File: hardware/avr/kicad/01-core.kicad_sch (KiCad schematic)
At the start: 18 parts, among them U1 ATmega1284P-PU, Y1 8MHz

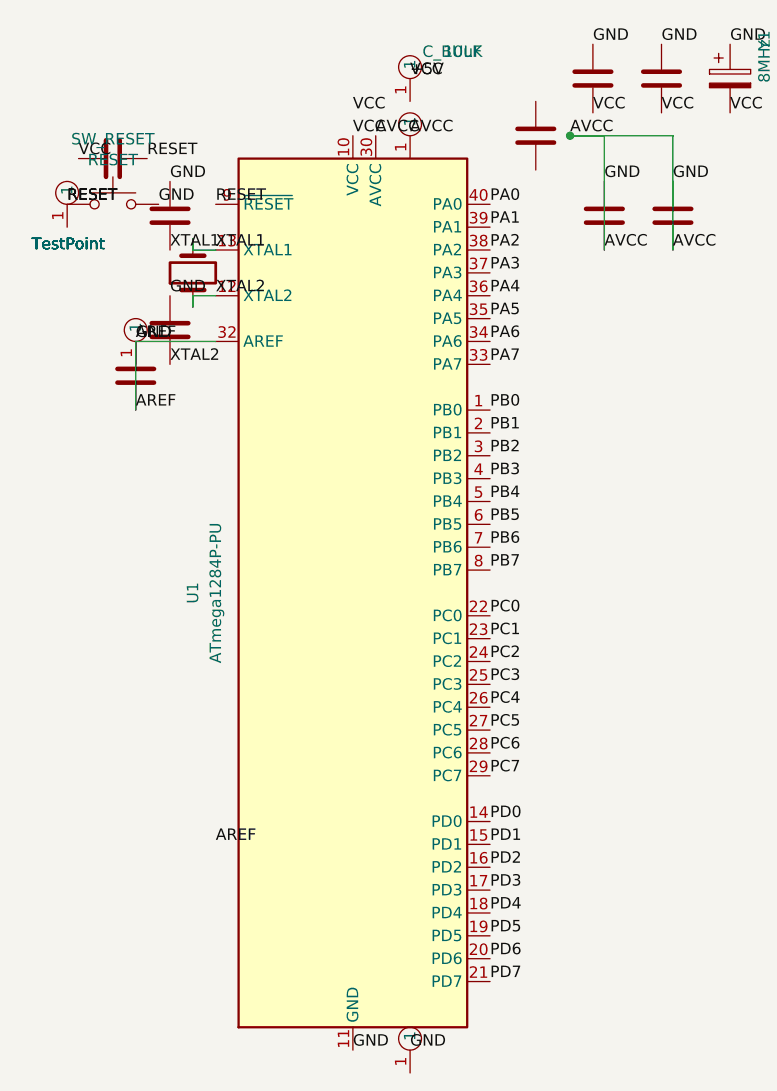
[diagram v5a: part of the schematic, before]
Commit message: Normalize embedded AVR symbol pin geometry
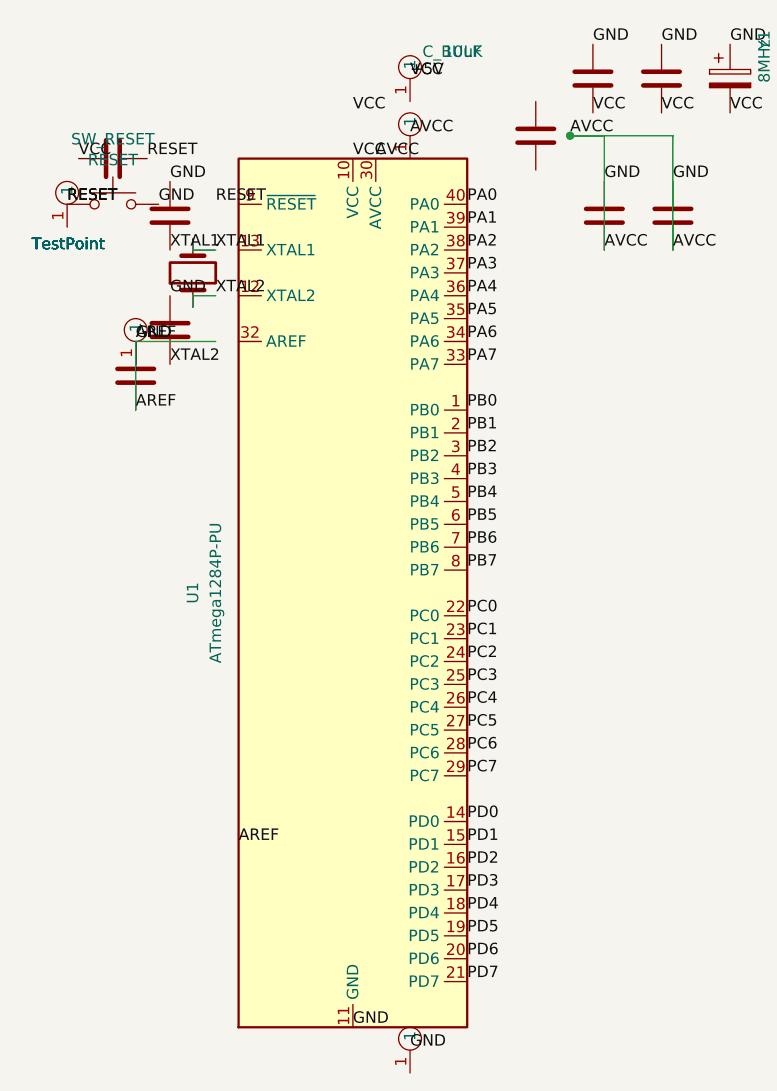
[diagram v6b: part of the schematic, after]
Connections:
- net AREF: no longer U1.32 (AREF)
- net RESET: no longer U1.9 (~{RESET})
- net XTAL1: no longer U1.13 (XTAL1)
- net XTAL2: no longer U1.12 (XTAL2)
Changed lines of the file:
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@@
 (kicad_sch (version 20230121) (generator eeschema)
   (paper "A4")
-  (label "VCC" (at 57.15 29.21 0) (fields_autoplaced)
-    (effects (font (size 1.27 1.27)) (justify left bottom))
-  )
-  (label "GND" (at 57.15 130.81 0) (fields_autoplaced)
-    (effects (font (size 1.27 1.27)) (justify left bottom))
-  )
-  (label "AVCC" (at 59.69 29.21 0) (fields_autoplaced)
-    (effects (font (size 1.27 1.27)) (justify left bottom))
-  )
-  (label "AREF" (at 41.91 107.95 0) (fields_autoplaced)
+  (label "VCC" (at 57.15 31.75 0) (fields_autoplaced)
+    (effects (font (size 1.27 1.27)) (justify left bottom))
+  )
+  (label "GND" (at 57.15 128.27 0) (fields_autoplaced)
+    (effects (font (size 1.27 1.27)) (justify left bottom))
+  )
+  (label "AVCC" (at 59.69 31.75 0) (fields_autoplaced)
+    (effects (font (size 1.27 1.27)) (justify left bottom))
+  )
+  (label "AREF" (at 44.45 107.95 0) (fields_autoplaced)
     (effects (font (size 1.27 1.27)) (justify left bottom))
   )
@@
     )
   )
-  (label "PA0" (at 72.39 36.83 0) (fields_autoplaced)
-    (effects (font (size 1.27 1.27)) (justify left bottom))
-  )
-  (label "PA1" (at 72.39 39.37 0) (fields_autoplaced)
-    (effects (font (size 1.27 1.27)) (justify left bottom))
-  )
-  (label "PA2" (at 72.39 41.91 0) (fields_autoplaced)
-    (effects (font (size 1.27 1.27)) (justify left bottom))
-  )
-  (label "PA3" (at 72.39 44.45 0) (fields_autoplaced)
-    (effects (font (size 1.27 1.27)) (justify left bottom))
-  )
-  (label "PA4" (at 72.39 46.99 0) (fields_autoplaced)
-    (effects (font (size 1.27 1.27)) (justify left bottom))
-  )
-  (label "PA5" (at 72.39 49.53 0) (fields_autoplaced)
-    (effects (font (size 1.27 1.27)) (justify left bottom))
-  )
-  (label "PA6" (at 72.39 52.07 0) (fields_autoplaced)
-    (effects (font (size 1.27 1.27)) (justify left bottom))
-  )
-  (label "PA7" (at 72.39 54.61 0) (fields_autoplaced)
-    (effects (font (size 1.27 1.27)) (justify left bottom))
-  )
-  (label "PB0" (at 72.39 59.69 0) (fields_autoplaced)
-    (effects (font (size 1.27 1.27)) (justify left bottom))
-  )
-  (label "PB1" (at 72.39 62.23 0) (fields_autoplaced)
-    (effects (font (size 1.27 1.27)) (justify left bottom))
-  )
-  (label "PB2" (at 72.39 64.77 0) (fields_autoplaced)
-    (effects (font (size 1.27 1.27)) (justify left bottom))
-  )
-  (label "PB3" (at 72.39 67.31 0) (fields_autoplaced)
-    (effects (font (size 1.27 1.27)) (justify left bottom))
-  )
-  (label "PB4" (at 72.39 69.85 0) (fields_autoplaced)
-    (effects (font (size 1.27 1.27)) (justify left bottom))
-  )
-  (label "PB5" (at 72.39 72.39 0) (fields_autoplaced)
-    (effects (font (size 1.27 1.27)) (justify left bottom))
-  )
-  (label "PB6" (at 72.39 74.93 0) (fields_autoplaced)
-    (effects (font (size 1.27 1.27)) (justify left bottom))
-  )
-  (label "PB7" (at 72.39 77.47 0) (fields_autoplaced)
-    (effects (font (size 1.27 1.27)) (justify left bottom))
-  )
-  (label "PC0" (at 72.39 82.55 0) (fields_autoplaced)
-    (effects (font (size 1.27 1.27)) (justify left bottom))
-  )
-  (label "PC1" (at 72.39 85.09 0) (fields_autoplaced)
-    (effects (font (size 1.27 1.27)) (justify left bottom))
-  )
-  (label "PC2" (at 72.39 87.63 0) (fields_autoplaced)
-    (effects (font (size 1.27 1.27)) (justify left bottom))
-  )
-  (label "PC3" (at 72.39 90.17 0) (fields_autoplaced)
-    (effects (font (size 1.27 1.27)) (justify left bottom))
-  )
-  (label "PC4" (at 72.39 92.71 0) (fields_autoplaced)
-    (effects (font (size 1.27 1.27)) (justify left bottom))
-  )
-  (label "PC5" (at 72.39 95.25 0) (fields_autoplaced)
-    (effects (font (size 1.27 1.27)) (justify left bottom))
-  )
-  (label "PC6" (at 72.39 97.79 0) (fields_autoplaced)
-    (effects (font (size 1.27 1.27)) (justify left bottom))
-  )
-  (label "PC7" (at 72.39 100.33 0) (fields_autoplaced)
-    (effects (font (size 1.27 1.27)) (justify left bottom))
-  )
-  (label "PD0" (at 72.39 105.41 0) (fields_autoplaced)
-    (effects (font (size 1.27 1.27)) (justify left bottom))
-  )
-  (label "PD1" (at 72.39 107.95 0) (fields_autoplaced)
-    (effects (font (size 1.27 1.27)) (justify left bottom))
-  )
-  (label "PD2" (at 72.39 110.49 0) (fields_autoplaced)
-    (effects (font (size 1.27 1.27)) (justify left bottom))
-  )
-  (label "PD3" (at 72.39 113.03 0) (fields_autoplaced)
-    (effects (font (size 1.27 1.27)) (justify left bottom))
-  )
-  (label "PD4" (at 72.39 115.57 0) (fields_autoplaced)
-    (effects (font (size 1.27 1.27)) (justify left bottom))
-  )
-  (label "PD5" (at 72.39 118.11 0) (fields_autoplaced)
-    (effects (font (size 1.27 1.27)) (justify left bottom))
-  )
-  (label "PD6" (at 72.39 120.65 0) (fields_autoplaced)
-    (effects (font (size 1.27 1.27)) (justify left bottom))
-  )
-  (label "PD7" (at 72.39 123.19 0) (fields_autoplaced)
-    (effects (font (size 1.27 1.27)) (justify left bottom))
-  )
+  (label "PA0" (at 69.85 36.83 0) (fields_autoplaced)
+    (effects (font (size 1.27 1.27)) (justify left bottom))
+  )
+  (label "PA1" (at 69.85 39.37 0) (fields_autoplaced)
+    (effects (font (size 1.27 1.27)) (justify left bottom))
+  )
+  (label "PA2" (at 69.85 41.91 0) (fields_autoplaced)
+    (effects (font (size 1.27 1.27)) (justify left bottom))
+  )
+  (label "PA3" (at 69.85 44.45 0) (fields_autoplaced)
+    (effects (font (size 1.27 1.27)) (justify left bottom))
+  )
+  (label "PA4" (at 69.85 46.99 0) (fields_autoplaced)
+    (effects (font (size 1.27 1.27)) (justify left bottom))
+  )
+  (label "PA5" (at 69.85 49.53 0) (fields_autoplaced)
+    (effects (font (size 1.27 1.27)) (justify left bottom))
+  )
+  (label "PA6" (at 69.85 52.07 0) (fields_autoplaced)
+    (effects (font (size 1.27 1.27)) (justify left bottom))
+  )
+  (label "PA7" (at 69.85 54.61 0) (fields_autoplaced)
+    (effects (font (size 1.27 1.27)) (justify left bottom))
+  )
+  (label "PB0" (at 69.85 59.69 0) (fields_autoplaced)
+    (effects (font (size 1.27 1.27)) (justify left bottom))
+  )
+  (label "PB1" (at 69.85 62.23 0) (fields_autoplaced)
+    (effects (font (size 1.27 1.27)) (justify left bottom))
+  )
+  (label "PB2" (at 69.85 64.77 0) (fields_autoplaced)
+    (effects (font (size 1.27 1.27)) (justify left bottom))
+  )
+  (label "PB3" (at 69.85 67.31 0) (fields_autoplaced)
+    (effects (font (size 1.27 1.27)) (justify left bottom))
+  )
+  (label "PB4" (at 69.85 69.85 0) (fields_autoplaced)
+    (effects (font (size 1.27 1.27)) (justify left bottom))
+  )
+  (label "PB5" (at 69.85 72.39 0) (fields_autoplaced)
+    (effects (font (size 1.27 1.27)) (justify left bottom))
+  )
+  (label "PB6" (at 69.85 74.93 0) (fields_autoplaced)
+    (effects (font (size 1.27 1.27)) (justify left bottom))
+  )
+  (label "PB7" (at 69.85 77.47 0) (fields_autoplaced)
+    (effects (font (size 1.27 1.27)) (justify left bottom))
+  )
+  (label "PC0" (at 69.85 82.55 0) (fields_autoplaced)
+    (effects (font (size 1.27 1.27)) (justify left bottom))
+  )
+  (label "PC1" (at 69.85 85.09 0) (fields_autoplaced)
+    (effects (font (size 1.27 1.27)) (justify left bottom))
+  )
+  (label "PC2" (at 69.85 87.63 0) (fields_autoplaced)
+    (effects (font (size 1.27 1.27)) (justify left bottom))
+  )
+  (label "PC3" (at 69.85 90.17 0) (fields_autoplaced)
+    (effects (font (size 1.27 1.27)) (justify left bottom))
+  )
+  (label "PC4" (at 69.85 92.71 0) (fields_autoplaced)
+    (effects (font (size 1.27 1.27)) (justify left bottom))
+  )
+  (label "PC5" (at 69.85 95.25 0) (fields_autoplaced)
+    (effects (font (size 1.27 1.27)) (justify left bottom))
+  )
+  (label "PC6" (at 69.85 97.79 0) (fields_autoplaced)
+    (effects (font (size 1.27 1.27)) (justify left bottom))
+  )
+  (label "PC7" (at 69.85 100.33 0) (fields_autoplaced)
+    (effects (font (size 1.27 1.27)) (justify left bottom))
+  )
+  (label "PD0" (at 69.85 105.41 0) (fields_autoplaced)
+    (effects (font (size 1.27 1.27)) (justify left bottom))
+  )
+  (label "PD1" (at 69.85 107.95 0) (fields_autoplaced)
+    (effects (font (size 1.27 1.27)) (justify left bottom))
+  )
+  (label "PD2" (at 69.85 110.49 0) (fields_autoplaced)
+    (effects (font (size 1.27 1.27)) (justify left bottom))
+  )
+  (label "PD3" (at 69.85 113.03 0) (fields_autoplaced)
+    (effects (font (size 1.27 1.27)) (justify left bottom))
+  )
+  (label "PD4" (at 69.85 115.57 0) (fields_autoplaced)
+    (effects (font (size 1.27 1.27)) (justify left bottom))
+  )
+  (label "PD5" (at 69.85 118.11 0) (fields_autoplaced)
+    (effects (font (size 1.27 1.27)) (justify left bottom))
+  )
+  (label "PD6" (at 69.85 120.65 0) (fields_autoplaced)
+    (effects (font (size 1.27 1.27)) (justify left bottom))
+  )
+  (label "PD7" (at 69.85 123.19 0) (fields_autoplaced)
+    (effects (font (size 1.27 1.27)) (justify left bottom))
+  )

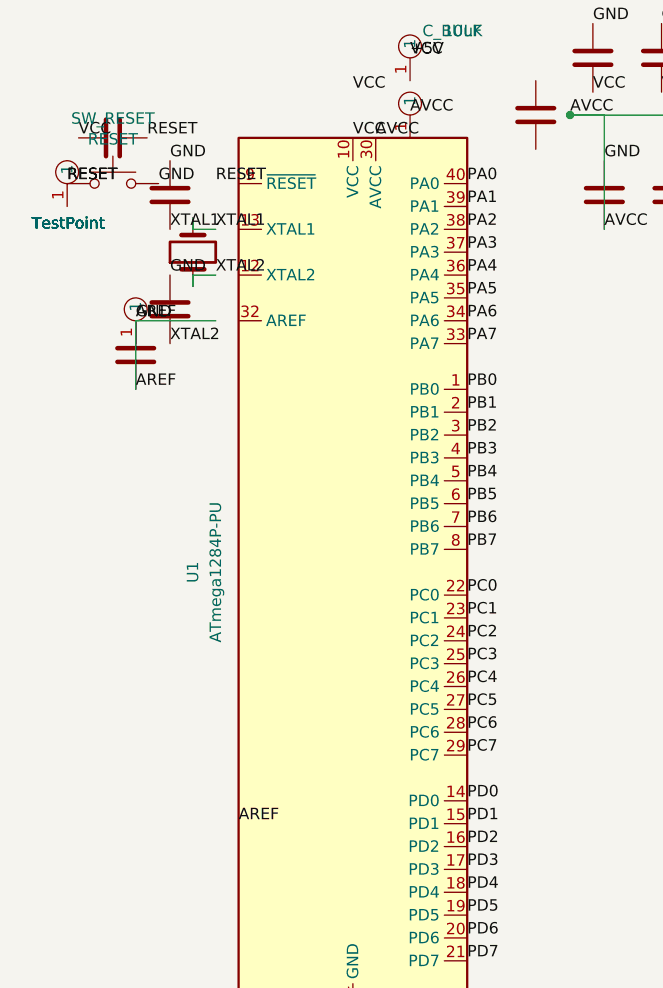
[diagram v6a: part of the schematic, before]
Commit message: Align AVR special-function labels to normalized pins
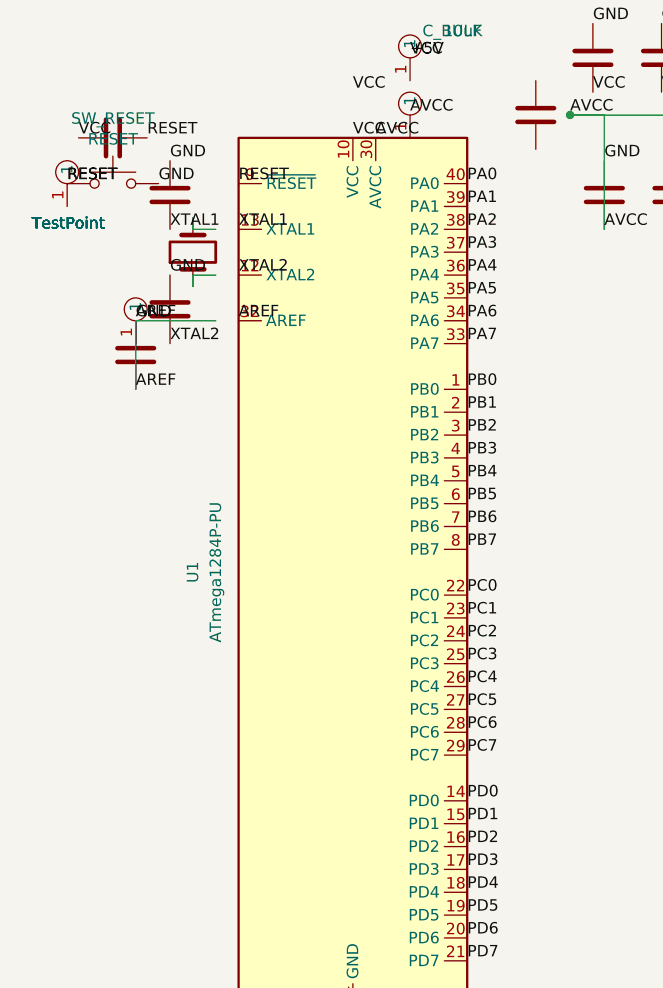
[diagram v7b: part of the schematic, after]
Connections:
- net AREF: now also U1.32 (AREF)
- net RESET: now also U1.9 (~{RESET})
- net XTAL1: now also U1.13 (XTAL1); no longer Y1.2
- net XTAL2: now also U1.12 (XTAL2); no longer Y1.1
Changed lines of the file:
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@@
     (effects (font (size 1.27 1.27)) (justify left bottom))
   )
-  (label "AREF" (at 44.45 107.95 0) (fields_autoplaced)
+  (label "AREF" (at 44.45 52.07 0) (fields_autoplaced)
     (effects (font (size 1.27 1.27)) (justify left bottom))
   )
-  (label "RESET" (at 41.91 36.83 0) (fields_autoplaced)
+  (label "RESET" (at 44.45 36.83 0) (fields_autoplaced)
     (effects (font (size 1.27 1.27)) (justify left bottom))
   )
-  (label "XTAL1" (at 41.91 41.91 0) (fields_autoplaced)
+  (label "XTAL1" (at 44.45 41.91 0) (fields_autoplaced)
     (effects (font (size 1.27 1.27)) (justify left bottom))
   )
-  (label "XTAL2" (at 41.91 46.99 0) (fields_autoplaced)
+  (label "XTAL2" (at 44.45 46.99 0) (fields_autoplaced)
     (effects (font (size 1.27 1.27)) (justify left bottom))
   )
